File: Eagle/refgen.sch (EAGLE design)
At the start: 22 parts, among them IC2 MAX6341N

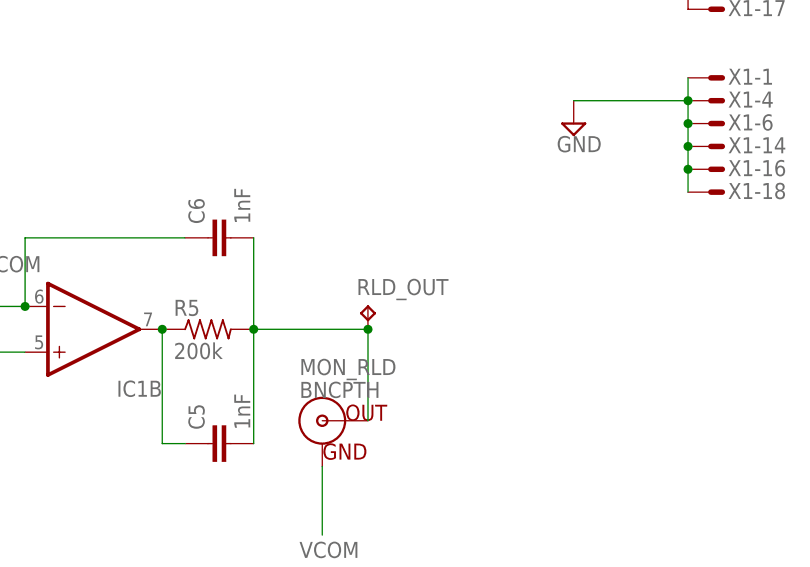
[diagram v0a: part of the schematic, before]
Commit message: Added DIN 42802 jacks & power for active electrodes
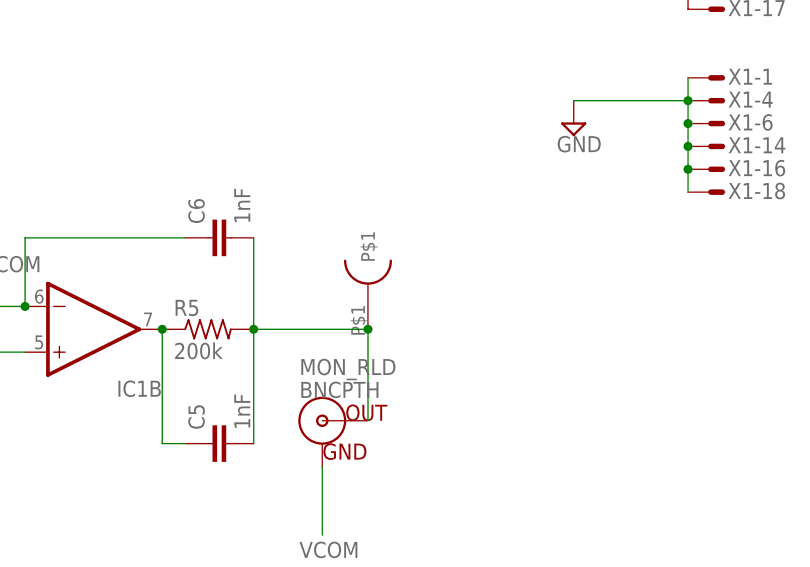
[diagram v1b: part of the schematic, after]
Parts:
- RLD_OUT: value TPPAD1-17 -> DIN42802; device testpad:TPPAD1-17 -> modEEG:DIN42802
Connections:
- net N$5: now also RLD_OUT.P$1; no longer RLD_OUT.TP
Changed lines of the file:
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@@
 <part name="C6" library="resistor" deviceset="C-EU" device="050-025X075" value="1nF"/>
 <part name="SUPPLY8" library="supply2" deviceset="GND" device=""/>
-<part name="RLD_OUT" library="testpad" deviceset="TP" device="PAD1-17"/>
 <part name="VCOM" library="testpad" deviceset="TP" device="PAD1-17"/>
 <part name="SUPPLY9" library="supply2" deviceset="GND" device=""/>
@@
 <part name="RLD_COM" library="testpad" deviceset="TP" device="PAD1-17"/>
 <part name="C9" library="resistor" deviceset="C-EU" device="050-025X075" value="0.01uf"/>
+<part name="RLD_OUT" library="modEEG" deviceset="DIN42802" device=""/>
 </parts>
 <sheets>
@@
 <instance part="C6" gate="G$1" x="58.42" y="0" rot="R90"/>
 <instance part="SUPPLY8" gate="GND" x="12.7" y="-20.32"/>
-<instance part="RLD_OUT" gate="G$1" x="76.2" y="-7.62"/>
 <instance part="VCOM" gate="G$1" x="2.54" y="-5.08"/>
 <instance part="SUPPLY9" gate="GND" x="119.38" y="50.8"/>
@@
 <instance part="RLD_COM" gate="G$1" x="30.48" y="-5.08"/>
 <instance part="C9" gate="G$1" x="-30.48" y="63.5"/>
+<instance part="RLD_OUT" gate="G$1" x="76.2" y="-10.16" rot="R90"/>
 </instances>
 <busses>
@@
 <wire x1="63.5" y1="-10.16" x2="63.5" y2="0" width="0.1524" layer="91"/>
 <junction x="63.5" y="-10.16"/>
-<pinref part="RLD_OUT" gate="G$1" pin="TP"/>
 <wire x1="63.5" y1="-10.16" x2="76.2" y2="-10.16" width="0.1524" layer="91"/>
 <pinref part="MON_RLD" gate="G$1" pin="OUT"/>
 <wire x1="76.2" y1="-20.32" x2="76.2" y2="-10.16" width="0.1524" layer="91"/>
+<pinref part="RLD_OUT" gate="G$1" pin="P$1"/>
 <junction x="76.2" y="-10.16"/>
 </segment>

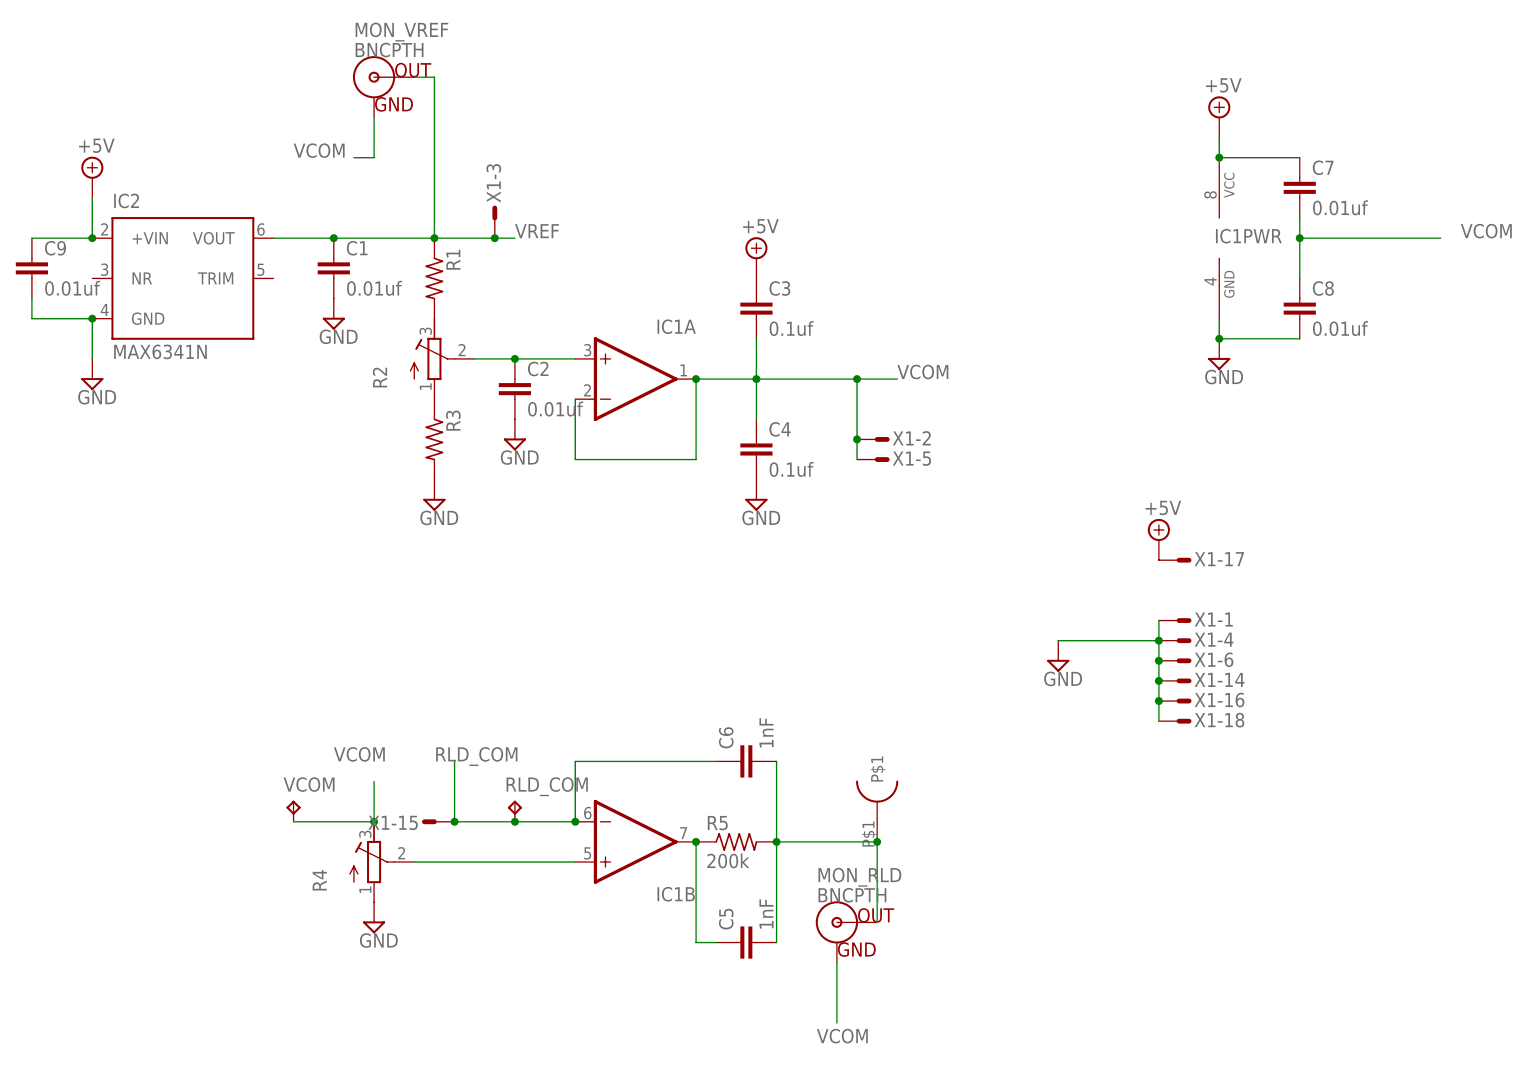
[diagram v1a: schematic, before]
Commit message: Board shrink
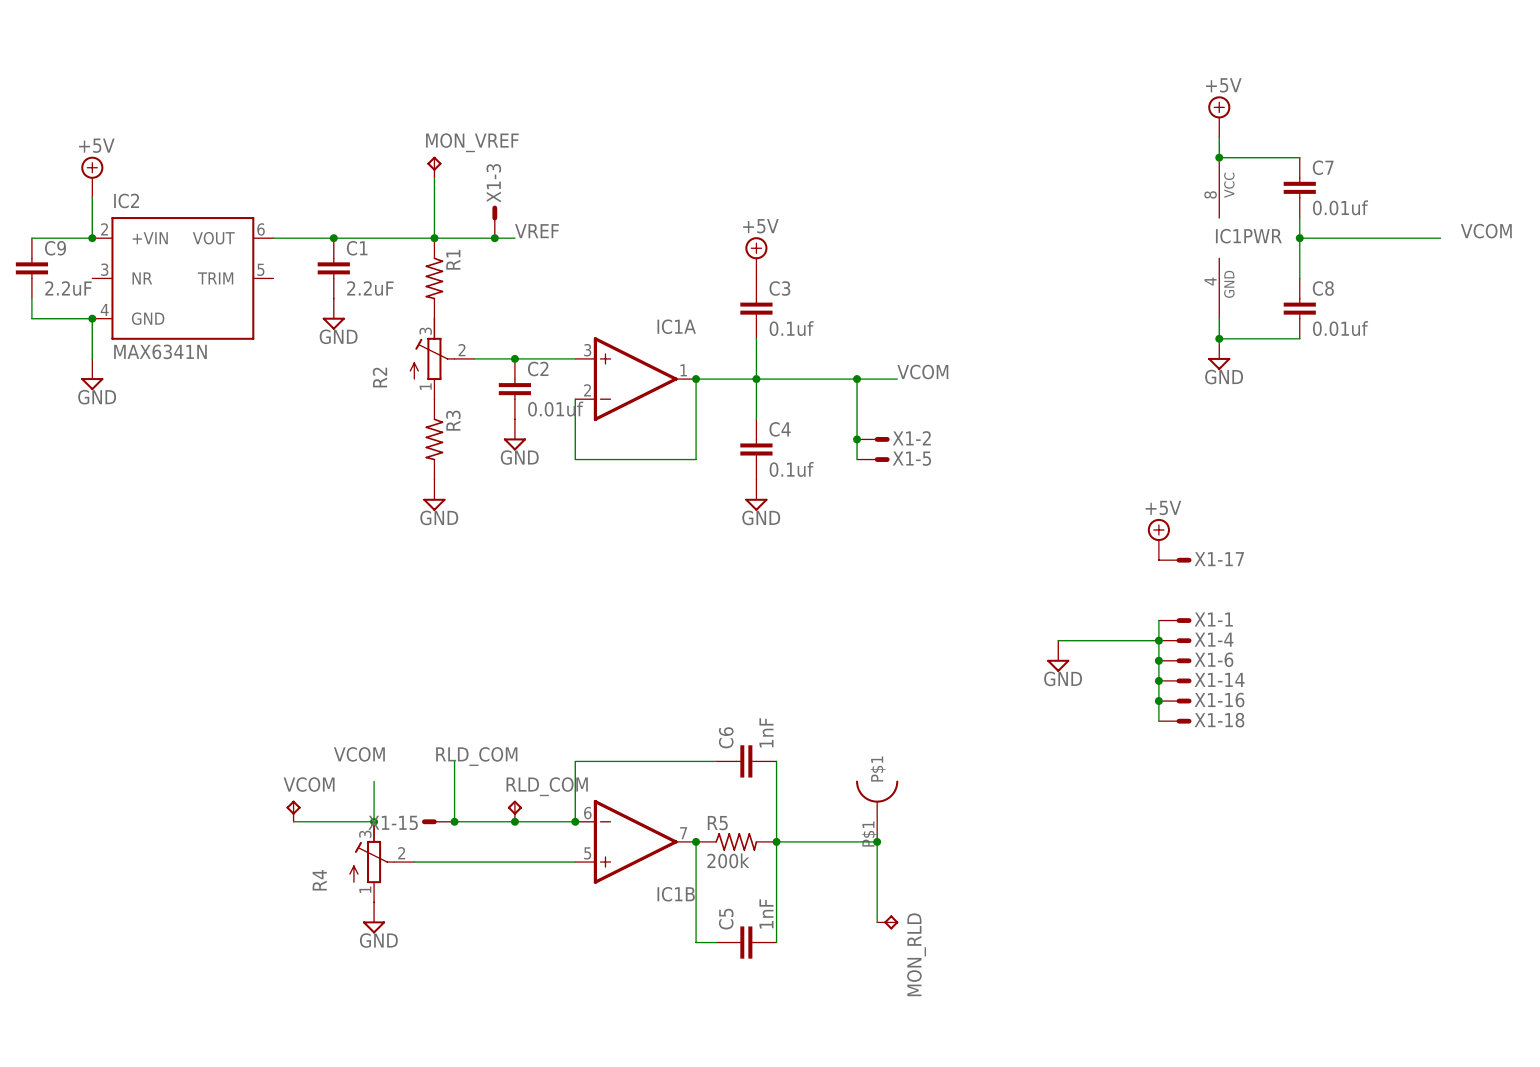
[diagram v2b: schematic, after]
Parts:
- C1, C9: value 0.01uf -> 2.2uF
- MON_RLD, MON_VREF: value BNCPTH -> TPPAD1-17; device SparkFun-Connectors:BNCPTH -> testpad:TPPAD1-17
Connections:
- net N$5: now also MON_RLD.TP; no longer MON_RLD.OUT
- net VCOM: no longer MON_RLD.GND, MON_VREF.GND
- net VREF: now also MON_VREF.TP; no longer MON_VREF.OUT
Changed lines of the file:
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@@
 <part name="SUPPLY1" library="supply2" deviceset="+5V" device=""/>
 <part name="SUPPLY2" library="supply2" deviceset="GND" device=""/>
-<part name="C1" library="resistor" deviceset="C-EU" device="050-025X075" value="0.01uf"/>
+<part name="C1" library="resistor" deviceset="C-EU" device="050-025X075" value="2.2uF"/>
 <part name="R1" library="resistor" deviceset="R-US_" device="0204/2V"/>
 <part name="R2" library="resistor" deviceset="R-TRIMM" device="3296W"/>
@@
 <part name="SUPPLY11" library="supply2" deviceset="GND" device=""/>
 <part name="SUPPLY12" library="supply2" deviceset="+5V" device=""/>
-<part name="MON_VREF" library="SparkFun-Connectors" deviceset="BNC" device="PTH"/>
-<part name="MON_RLD" library="SparkFun-Connectors" deviceset="BNC" device="PTH"/>
 <part name="RLD_COM" library="testpad" deviceset="TP" device="PAD1-17"/>
-<part name="C9" library="resistor" deviceset="C-EU" device="050-025X075" value="0.01uf"/>
+<part name="C9" library="resistor" deviceset="C-EU" device="050-025X075" value="2.2uF"/>
 <part name="RLD_OUT" library="modEEG" deviceset="DIN42802" device=""/>
+<part name="MON_RLD" library="testpad" deviceset="TP" device="PAD1-17"/>
+<part name="MON_VREF" library="testpad" deviceset="TP" device="PAD1-17"/>
 </parts>
 <sheets>
@@
 <instance part="SUPPLY11" gate="GND" x="99.06" y="12.7"/>
 <instance part="SUPPLY12" gate="+5V" x="111.76" y="27.94"/>
-<instance part="MON_VREF" gate="G$1" x="12.7" y="86.36"/>
-<instance part="MON_RLD" gate="G$1" x="71.12" y="-20.32"/>
 <instance part="RLD_COM" gate="G$1" x="30.48" y="-5.08"/>
 <instance part="C9" gate="G$1" x="-30.48" y="63.5"/>
 <instance part="RLD_OUT" gate="G$1" x="76.2" y="-10.16" rot="R90"/>
+<instance part="MON_RLD" gate="G$1" x="78.74" y="-20.32" rot="R270"/>
+<instance part="MON_VREF" gate="G$1" x="20.32" y="76.2"/>
 </instances>
 <busses>
@@
 <wire x1="27.94" y1="66.04" x2="30.48" y2="66.04" width="0.1524" layer="91"/>
 <junction x="27.94" y="66.04"/>
-<pinref part="MON_VREF" gate="G$1" pin="OUT"/>
-<wire x1="17.78" y1="86.36" x2="20.32" y2="86.36" width="0.1524" layer="91"/>
-<wire x1="20.32" y1="86.36" x2="20.32" y2="66.04" width="0.1524" layer="91"/>
+<wire x1="20.32" y1="73.66" x2="20.32" y2="66.04" width="0.1524" layer="91"/>
+<pinref part="MON_VREF" gate="G$1" pin="TP"/>
 </segment>
 </net>
@@
 <label x="149.86" y="66.04" size="1.778" layer="95"/>
 </segment>
-<segment>
-<pinref part="MON_VREF" gate="G$1" pin="GND"/>
-<wire x1="12.7" y1="81.28" x2="12.7" y2="76.2" width="0.1524" layer="91"/>
-<wire x1="12.7" y1="76.2" x2="10.16" y2="76.2" width="0.1524" layer="91"/>
-<label x="2.54" y="76.2" size="1.778" layer="95"/>
-</segment>
-<segment>
-<pinref part="MON_RLD" gate="G$1" pin="GND"/>
-<wire x1="71.12" y1="-25.4" x2="71.12" y2="-33.02" width="0.1524" layer="91"/>
-<label x="68.58" y="-35.56" size="1.778" layer="95"/>
-</segment>
 </net>
 <net name="RLD_COM" class="0">
@@
 <junction x="63.5" y="-10.16"/>
 <wire x1="63.5" y1="-10.16" x2="76.2" y2="-10.16" width="0.1524" layer="91"/>
-<pinref part="MON_RLD" gate="G$1" pin="OUT"/>
 <wire x1="76.2" y1="-20.32" x2="76.2" y2="-10.16" width="0.1524" layer="91"/>
 <pinref part="RLD_OUT" gate="G$1" pin="P$1"/>
 <junction x="76.2" y="-10.16"/>
-</segment>
-</net>
+<pinref part="MON_RLD" gate="G$1" pin="TP"/>
+</segment>
+</net>
